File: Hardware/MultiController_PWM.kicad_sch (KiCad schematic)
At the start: 13 parts, among them T1 BSS138DW, U5 LM358

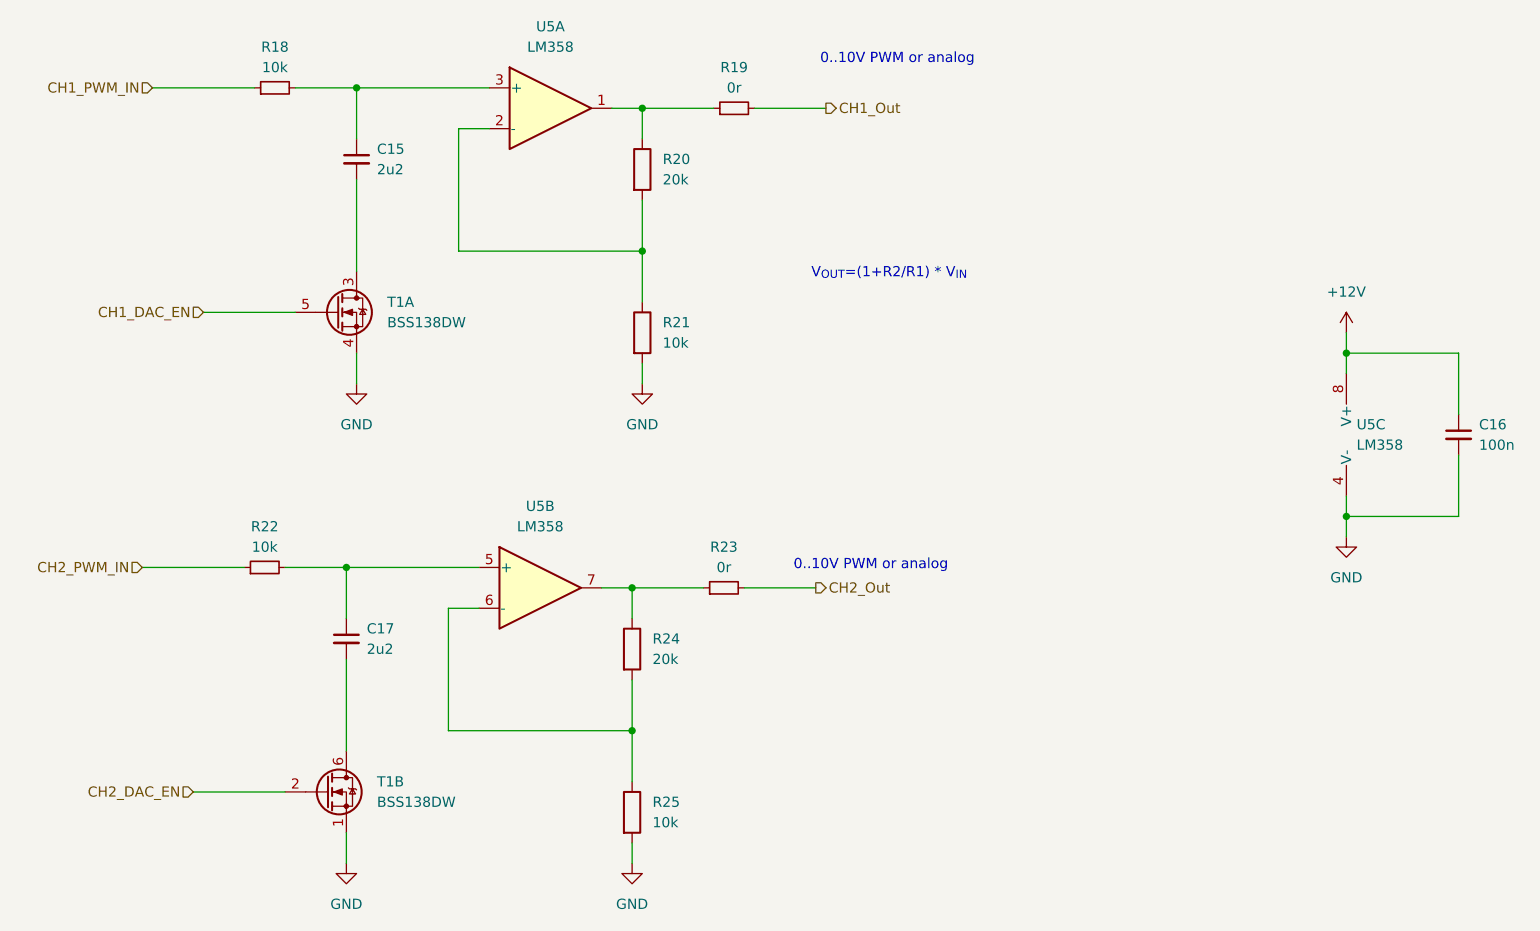
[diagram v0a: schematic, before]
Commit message: changed OP Amps to Rail-to-Rail type fix #8
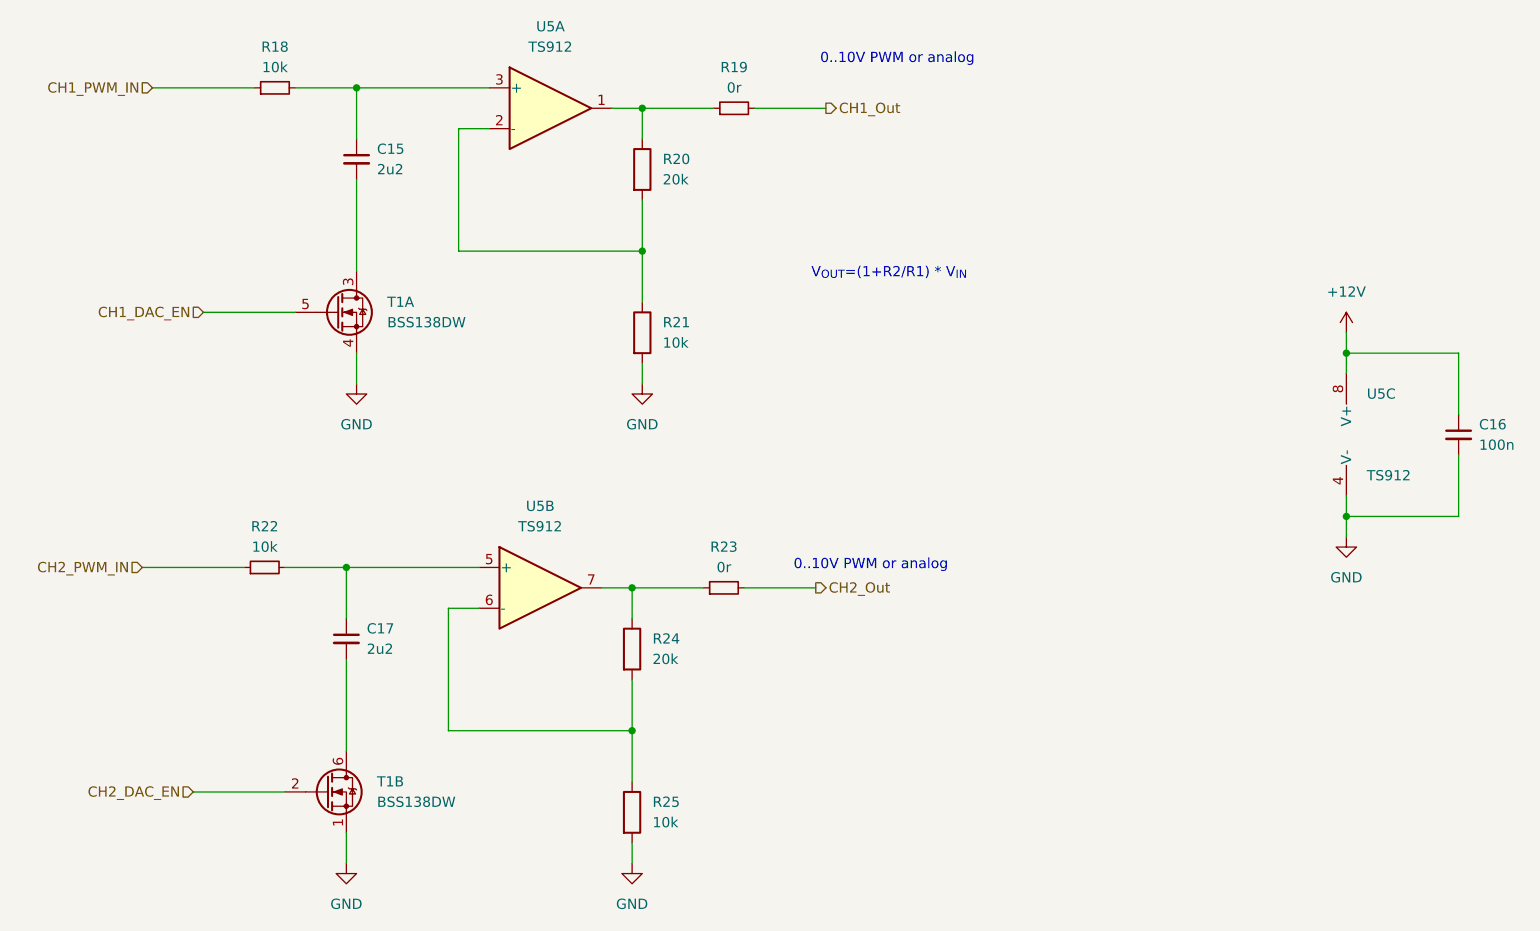
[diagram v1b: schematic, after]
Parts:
- U5: value LM358 -> TS912; symbol Amplifier_Operational:LM358 -> Amplifier_Operational:TS912; JLCPCB Part # C9418 -> C73655; MPN LM358DT -> TS912IDT
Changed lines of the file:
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@@
 	)
 	(symbol
-		(lib_id "Amplifier_Operational:LM358")
+		(lib_id "Amplifier_Operational:TS912")
 		(at 100.33 102.87 0)
 		(unit 2)
@@
 			)
 		)
-		(property "Value" "LM358"
+		(property "Value" "TS912"
 			(at 100.33 95.25 0)
 			(effects
@@
 			)
 		)
-		(property "Datasheet" "http://www.ti.com/lit/ds/symlink/lm2904-n.pdf"
+		(property "Datasheet" "www.st.com/resource/en/datasheet/ts912.pdf"
 			(at 100.33 102.87 0)
 			(effects
@@
 			)
 		)
-		(property "Description" "Low-Power, Dual Operational Amplifiers, DIP-8/SOIC-8/TO-99-8"
+		(property "Description" "Dual Rail-to-rail CMOS Operational Amplifier, DIP-8/SOIC-8"
 			(at 100.33 102.87 0)
 			(effects
@@
 			)
 		)
-		(property "MPN" "LM358DT"
+		(property "MPN" "TS912IDT"
 			(at 100.33 102.87 0)
 			(effects
@@
 			)
 		)
-		(property "JLCPCB Part #" "C9418"
+		(property "JLCPCB Part #" "C73655"
 			(at 100.33 102.87 0)
 			(effects
@@
 	)
 	(symbol
-		(lib_id "Amplifier_Operational:LM358")
+		(lib_id "Amplifier_Operational:TS912")
 		(at 203.2 83.82 0)
 		(unit 3)
@@
 		(dnp no)
 		(property "Reference" "U5"
-			(at 201.93 82.5499 0)
-			(effects
-				(font
-					(size 1.27 1.27)
-				)
-				(justify left)
-			)
-		)
-		(property "Value" "LM358"
-			(at 201.93 85.0899 0)
+			(at 203.2 78.74 0)
+			(effects
+				(font
+					(size 1.27 1.27)
+				)
+				(justify left)
+			)
+		)
+		(property "Value" "TS912"
+			(at 203.2 88.9 0)
 			(effects
 				(font
@@
 			)
 		)
-		(property "Datasheet" "http://www.ti.com/lit/ds/symlink/lm2904-n.pdf"
+		(property "Datasheet" "www.st.com/resource/en/datasheet/ts912.pdf"
 			(at 203.2 83.82 0)
 			(effects
@@
 			)
 		)
-		(property "Description" "Low-Power, Dual Operational Amplifiers, DIP-8/SOIC-8/TO-99-8"
+		(property "Description" "Dual Rail-to-rail CMOS Operational Amplifier, DIP-8/SOIC-8"
 			(at 203.2 83.82 0)
 			(effects
@@
 			)
 		)
-		(property "MPN" "LM358DT"
+		(property "MPN" "TS912IDT"
 			(at 203.2 83.82 0)
 			(effects
@@
 			)
 		)
-		(property "JLCPCB Part #" "C9418"
+		(property "JLCPCB Part #" "C73655"
 			(at 203.2 83.82 0)
 			(effects
@@
 	)
 	(symbol
-		(lib_id "Amplifier_Operational:LM358")
+		(lib_id "Amplifier_Operational:TS912")
 		(at 101.6 43.18 0)
 		(unit 1)
@@
 			)
 		)
-		(property "Value" "LM358"
+		(property "Value" "TS912"
 			(at 101.6 35.56 0)
 			(effects
@@
 			)
 		)
-		(property "Datasheet" "http://www.ti.com/lit/ds/symlink/lm2904-n.pdf"
+		(property "Datasheet" "www.st.com/resource/en/datasheet/ts912.pdf"
 			(at 101.6 43.18 0)
 			(effects
@@
 			)
 		)
-		(property "Description" "Low-Power, Dual Operational Amplifiers, DIP-8/SOIC-8/TO-99-8"
+		(property "Description" "Dual Rail-to-rail CMOS Operational Amplifier, DIP-8/SOIC-8"
 			(at 101.6 43.18 0)
 			(effects
@@
 			)
 		)
-		(property "MPN" "LM358DT"
+		(property "MPN" "TS912IDT"
 			(at 101.6 43.18 0)
 			(effects
@@
 			)
 		)
-		(property "JLCPCB Part #" "C9418"
+		(property "JLCPCB Part #" "C73655"
 			(at 101.6 43.18 0)
 			(effects

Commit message: fixed references
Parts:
- Q5: renamed from T1; JLCPCB Part # C5362112 -> C5362112 BSS138DW
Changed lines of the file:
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@@
 		(dnp no)
 		(fields_autoplaced yes)
-		(property "Reference" "T1"
+		(property "Reference" "Q5"
 			(at 81.28 67.3099 0)
 			(effects
@@
 			)
 		)
-		(property "JLCPCB Part #" "C5362112"
+		(property "JLCPCB Part #" "C5362112 BSS138DW "
 			(at 77.47 68.58 0)
 			(effects
@@
 			(project "MultiController"
 				(path "/252b555a-4cc8-4589-b58e-954efba9866f/5116a6a3-69cf-4233-b4f0-64a72a90e758"
-					(reference "T2")
+					(reference "Q6")
 					(unit 1)
 				)
 				(path "/252b555a-4cc8-4589-b58e-954efba9866f/ee0a951e-5eb3-4549-b988-1631d3ca164d"
-					(reference "T1")
+					(reference "Q5")
 					(unit 1)
 				)
@@
 		(dnp no)
 		(fields_autoplaced yes)
-		(property "Reference" "T1"
+		(property "Reference" "Q5"
 			(at 80.01 126.9999 0)
 			(effects
@@
 			)
 		)
-		(property "JLCPCB Part #" "C5362112"
+		(property "JLCPCB Part #" "C5362112 BSS138DW "
 			(at 76.2 128.27 0)
 			(effects
@@
 			(project "MultiController"
 				(path "/252b555a-4cc8-4589-b58e-954efba9866f/5116a6a3-69cf-4233-b4f0-64a72a90e758"
-					(reference "T2")
+					(reference "Q6")
 					(unit 2)
 				)
 				(path "/252b555a-4cc8-4589-b58e-954efba9866f/ee0a951e-5eb3-4549-b988-1631d3ca164d"
-					(reference "T1")
+					(reference "Q5")
 					(unit 2)
 				)
